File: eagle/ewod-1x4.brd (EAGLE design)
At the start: 40 x 40 mm, 24 parts

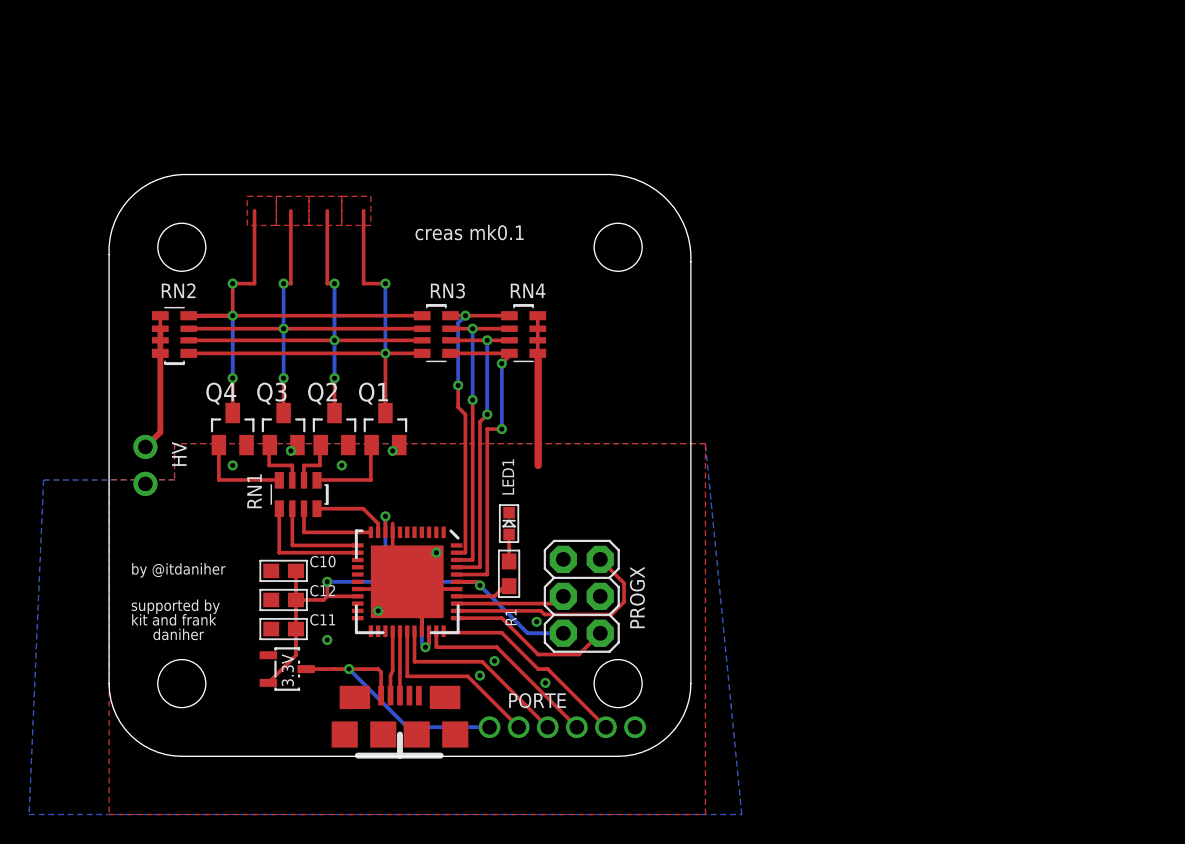
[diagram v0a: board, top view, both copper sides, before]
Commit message: redo to 50x50mm
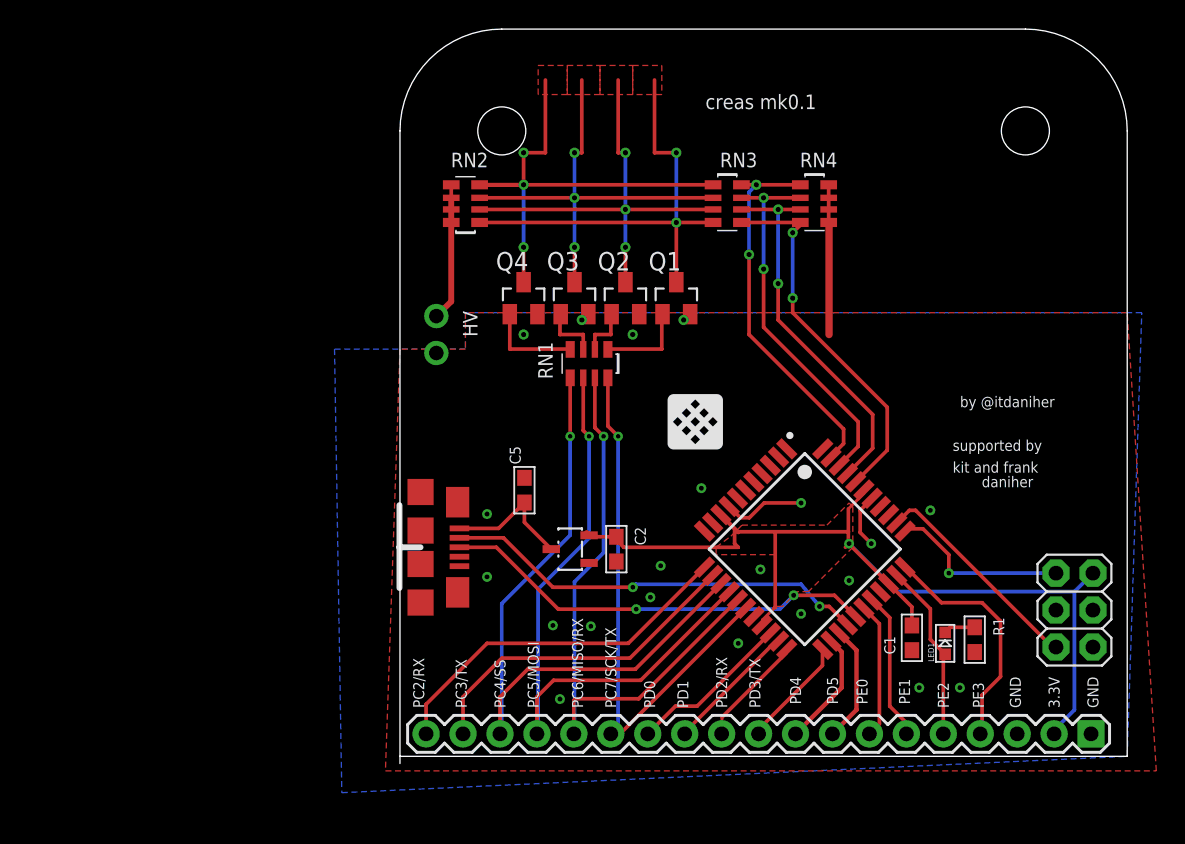
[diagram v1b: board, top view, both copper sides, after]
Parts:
- removed 3.3V: VREG, nonolith:SOT23-3
- removed C10: 1uF, nonolith:0603
- removed C11: .1uF, nonolith:0603
- removed C12: .01uF, nonolith:0603
- removed PORTE: (no value), nonolith:1X06_ROUND_2MM
- removed PROGX: (no value), nonolith:2X03
- removed U$3, U$4: (no value), nonolith:STAND-OFF
- removed XM1: (no value), nonolith:QFN-44
- added ATXMEGA32A4U: (no value), nonolith:TQFP-44
- added C1, C2, C5: (no value), nonolith:0603
- added JP1: (no value), nonolith:2X03
- added U$10: MCP1700, nonolith:SOT23-3
- added U$12: M19, SparkFun:1X19
- R1: value 120o -> (none)
- moved U$2 47.2 mm to (43.0, 43.0)
- moved U$1 43.9 mm to (7.00, 43.0)
- moved R1 32.3 mm to (39.5, 8.02), turned to 270 degrees
- moved LED1 31.1 mm to (37.5, 7.77)
- moved HV 21.9 mm to (2.50, 29.0)
- moved Q1 21.9 mm to (19.0, 31.5)
- moved Q2 21.9 mm to (15.5, 31.5)
- moved Q3 21.9 mm to (12.0, 31.5)
- moved Q4 21.9 mm to (8.50, 31.5)
- moved RN1 21.9 mm to (13.0, 27.0)
- moved RN2 21.9 mm to (4.50, 38.0)
- moved RN3 21.9 mm to (22.5, 38.0)
- moved RN4 21.9 mm to (28.5, 38.0)
- moved U$5 19.4 mm to (18.4, 21.1), flipped to the top
- moved CN1 12.9 mm to (1.41, 14.4), turned to 270 degrees
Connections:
- removed net 3.3V: 3.3V.2, C10.2, C11.2, C12.2, PROGX.2, XM1.19, XM1.31, XM1.39, XM1.9
- removed net 5V: 3.3V.3, CN1.P1, PORTE.1
- removed net ADCA: RN3.5, RN4.4, XM1.40
- removed net ADCB: RN3.6, RN4.3, XM1.41
- removed net ADCC: RN3.7, RN4.2, XM1.42
- removed net ADCD: RN3.8, RN4.1, XM1.43
- removed net BOOTLOAD: PROGX.4, XM1.36
- removed net OC0A: RN1.8, XM1.10
- removed net OC0B: RN1.7, XM1.11
- removed net OC0C: RN1.6, XM1.12
- removed net OC0D: RN1.5, XM1.13
- removed net PR1: R1.1, XM1.37
- removed net PR1-P: LED1.A, R1.2
- new net N$1: LED1.C, R1.1
- new net PA0: ATXMEGA32A4U.40, RN3.5, RN4.4
- new net PA1: ATXMEGA32A4U.41, RN3.6, RN4.3
- new net PA2: ATXMEGA32A4U.42, RN3.7, RN4.2
- new net PA3: ATXMEGA32A4U.43, RN3.8, RN4.1
- new net PA4: ATXMEGA32A4U.44
- new net PA5: ATXMEGA32A4U.1
- new net PA6: ATXMEGA32A4U.2
- new net PA7: ATXMEGA32A4U.3
- new net PB0: ATXMEGA32A4U.4
- new net PB1: ATXMEGA32A4U.5
- new net PB2: ATXMEGA32A4U.6
- new net PB3: ATXMEGA32A4U.7
- new net PC0: ATXMEGA32A4U.10
- new net PC1: ATXMEGA32A4U.11
- new net PC2: ATXMEGA32A4U.12, U$12.19
- new net PC3: ATXMEGA32A4U.13, U$12.18
- new net PC4: ATXMEGA32A4U.14, RN1.5, U$12.17
- new net PC5: ATXMEGA32A4U.15, RN1.6, U$12.16
- new net PC6: ATXMEGA32A4U.16, RN1.7, U$12.15
- new net PC7: ATXMEGA32A4U.17, RN1.8, U$12.14
- new net PD0: ATXMEGA32A4U.20, U$12.13
- new net PD1: ATXMEGA32A4U.21, U$12.12
- new net PD2: ATXMEGA32A4U.22, U$12.11
- new net PD3: ATXMEGA32A4U.23, U$12.10
- new net PD4: ATXMEGA32A4U.24, U$12.9
- new net PD5: ATXMEGA32A4U.25, U$12.8
- new net VCC: ATXMEGA32A4U.19, ATXMEGA32A4U.31, ATXMEGA32A4U.39, ATXMEGA32A4U.9, C1.1, C2.1, JP1.2, U$10.VOUT, U$12.2
- new net VUSB: C5.1, CN1.P1, U$10.VIN
- net GND: now also ATXMEGA32A4U.18, ATXMEGA32A4U.30, ATXMEGA32A4U.38, ATXMEGA32A4U.8, C1.2, C2.2, C5.2, JP1.6, R1.2, U$10.GND, U$12.1, U$12.3; no longer 3.3V.1, C10.1, C11.1, C12.1, LED1.C, PORTE.6, PROGX.6, XM1.18, XM1.30, XM1.38, XM1.8
- net PDI-CLK: now also ATXMEGA32A4U.35, JP1.5; no longer PROGX.5, XM1.35
- net PDI-DATA: now also ATXMEGA32A4U.34, JP1.1; no longer PROGX.1, XM1.34
- net PE0: now also ATXMEGA32A4U.28, U$12.7; no longer PORTE.2, XM1.28
- net PE1: now also ATXMEGA32A4U.29, U$12.6; no longer PORTE.3, XM1.29
- net PE2: now also ATXMEGA32A4U.32, LED1.A, U$12.5; no longer PORTE.4, XM1.32
- net PE3: now also ATXMEGA32A4U.33, U$12.4; no longer PORTE.5, XM1.33
- net USB+: now also ATXMEGA32A4U.27; no longer XM1.27
- net USB-: now also ATXMEGA32A4U.26; no longer XM1.26
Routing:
- net VCC: track 0.00 -> 71.4 mm, vias 0 -> 1
- net PC4: track 0.00 -> 47.4 mm, vias 0 -> 1
- net PC5: track 0.00 -> 44.9 mm, vias 0 -> 1
- net 3.3V: track 44.6 -> 0.00 mm, vias 4 -> 0
- net PC6: track 0.00 -> 42.0 mm, vias 0 -> 1
- net PC7: track 0.00 -> 37.8 mm, vias 0 -> 1
- net PA3: track 0.00 -> 26.0 mm, vias 0 -> 2
- net PA0: track 0.00 -> 25.8 mm, vias 0 -> 2
- net PA2: track 0.00 -> 25.7 mm, vias 0 -> 2
- net PA1: track 0.00 -> 25.6 mm, vias 0 -> 2
- net USB+: track 4.42 -> 30.0 mm, vias 0 -> 2
- net PC2: track 0.00 -> 25.1 mm
- net USB-: track 4.46 -> 29.4 mm, vias 0 -> 2
- net PC3: track 0.00 -> 23.2 mm
- net ADCA: track 22.7 -> 0.00 mm, vias 2 -> 0
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- added copper zone on layer 1, net VCC
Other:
- board size 40 x 40 mm -> 50 x 50.5 mm
- board text added: "3.3V"
- board text added: "ATxmega32A4U Breakout"
- board text added: "CC-By-SA"
- board text added: "GND"
- board text added: "Nonolith Labs"
- board text added: "PC2/RX"
- board text added: "PC3/TX"
- board text added: "PC4/SS"
- board text added: "PC5/MOSI"
- board text added: "PC6/MISO/RX"
- board text added: "PC7/SCK/TX"
- board text added: "PD0"
- board text added: "PD1"
- board text added: "PD2/RX"
- board text added: "PD3/TX"
- board text added: "PD4"
- board text added: "PD5"
- board text added: "PE0"
- board text added: "PE1"
- board text added: "PE2"
- board text added: "PE3"
- board text added: "Rev. 2.0"
- board text added: "nonolithlabs.com/breakout"

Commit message: final tweaks - fix drill width, add tenting, fix a few other things
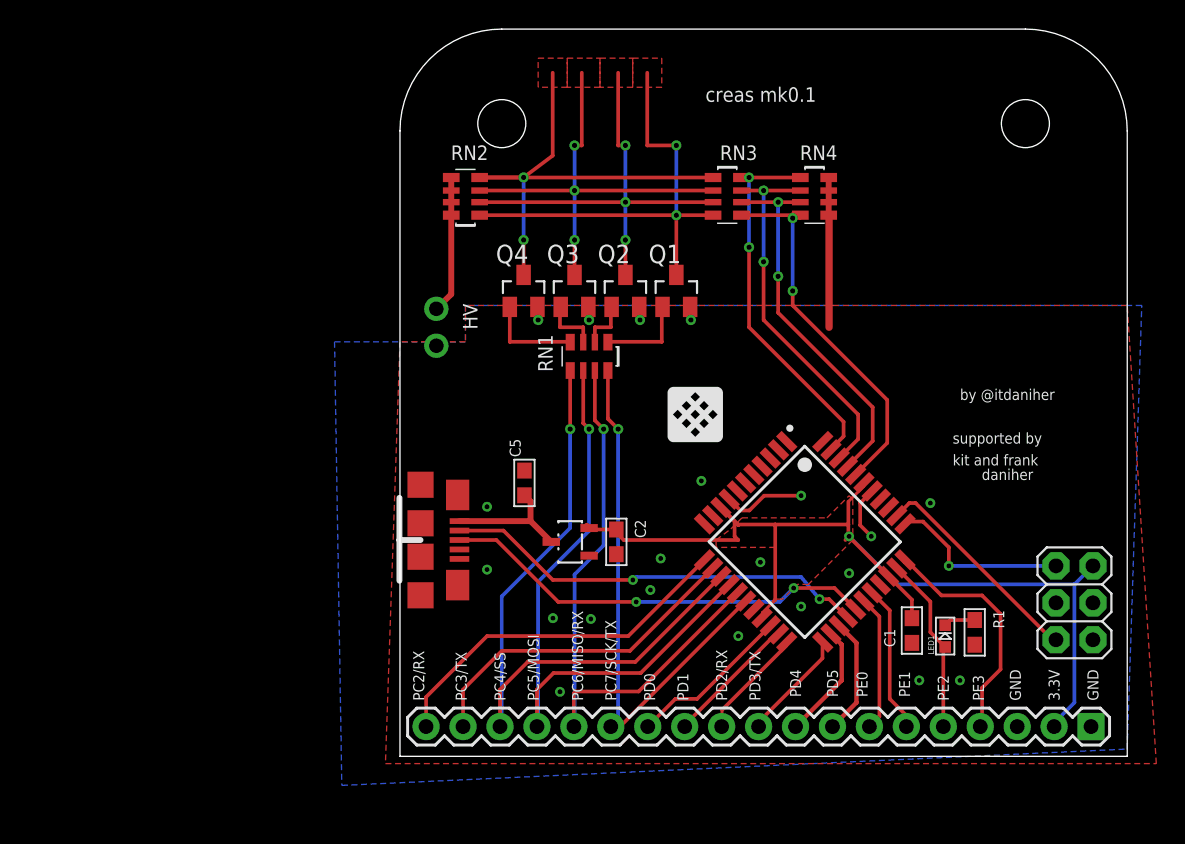
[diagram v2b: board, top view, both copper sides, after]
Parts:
- moved LED1 0.50 mm to (37.5, 8.27)
- moved ATXMEGA32A4U 0.50 mm to (27.8, 14.7)
- moved C1 0.50 mm to (35.2, 8.65)
- moved C2 0.50 mm to (14.9, 14.7)
- moved C5 0.50 mm to (8.56, 18.8)
- moved CN1 0.50 mm to (1.41, 14.9)
- moved HV 0.50 mm to (2.50, 29.5)
- moved JP1 0.50 mm to (46.4, 10.6)
- moved Q1 0.50 mm to (19.0, 32.0)
- moved Q2 0.50 mm to (15.5, 32.0)
- moved Q3 0.50 mm to (12.0, 32.0)
- moved Q4 0.50 mm to (8.50, 32.0)
- moved R1 0.50 mm to (39.5, 8.52)
- moved RN1 0.50 mm to (13.0, 27.5)
- moved RN2 0.50 mm to (4.50, 38.5)
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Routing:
- net VUSB: track 9.17 -> 11.5 mm
- net CELLD: track 34.5 -> 34.0 mm, vias 3 -> 2
- net CELLA: track 31.5 -> 32.0 mm
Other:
- board size 50 x 50.5 mm -> 50 x 50 mm
